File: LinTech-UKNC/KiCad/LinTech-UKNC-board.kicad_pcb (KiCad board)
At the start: 2 copper layers, 97 x 102.5 mm, 36 parts, among them J1 K2, Q1 КТ315Г, Y1 12MHz

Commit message: BOM
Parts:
- DD1: value 74LS00 -> i8031
- DD13: value 580DD55A -> 580VV55A
- J1: value K2 -> ~
- LAN1: value Conn_02x05_Odd_Even -> ОНП-КГ-56-10/33х7,4-В53
- WS1: value Conn_02x07_Counter_Clockwise -> ~

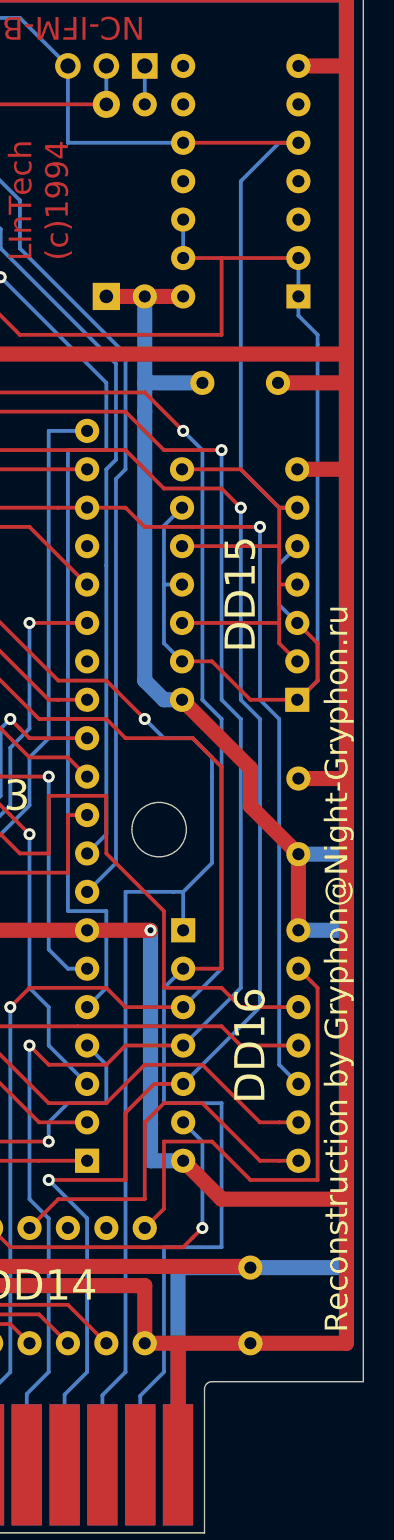
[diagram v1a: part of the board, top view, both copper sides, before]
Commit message: Fix footprint drill diameters
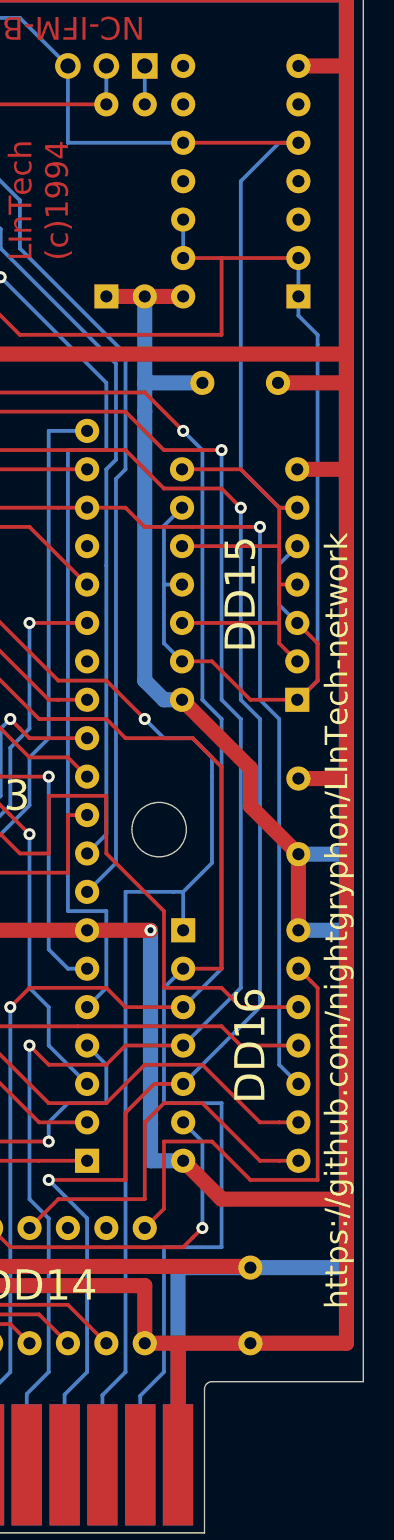
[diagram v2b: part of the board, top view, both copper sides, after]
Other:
- board text added: "https://github.com/nightgryphon/LInTech-network"
- board text removed: "Reconstruction by Gryphon@Night-Gryphon.ru"
